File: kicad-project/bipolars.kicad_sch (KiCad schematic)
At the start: 16 parts, among them J13 Conn_01x04_Male, J14 Conn_01x04_Male, J4 Conn_01x02_Female, J5 Conn_01x02_Female, J6 Conn_01x02_Female, J7 Conn_01x04_Male, J8 Conn_01x04_Male, J9 Conn_01x02_Female, U5 A4988_Shield, U6 A4988_Shield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

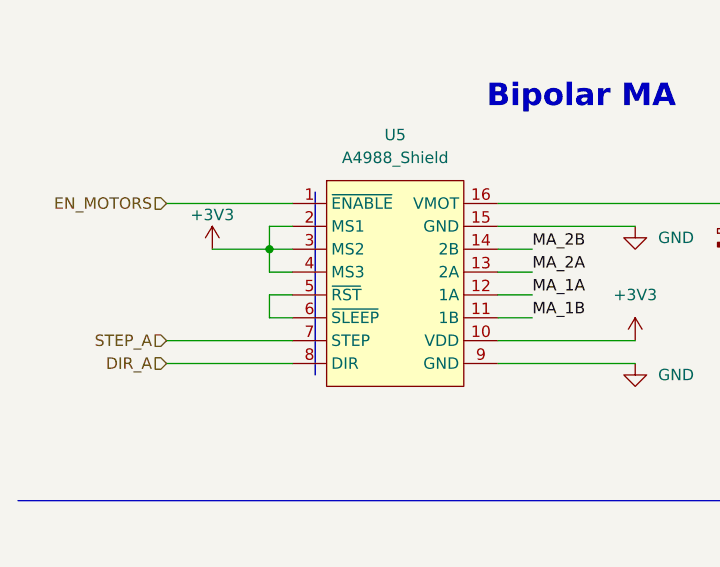
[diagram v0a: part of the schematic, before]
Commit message: hw: HSD v1.0 w/out peripherals
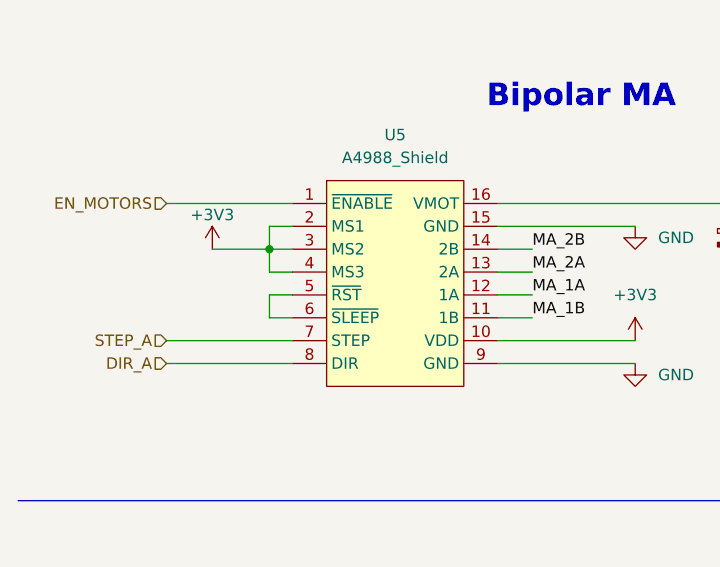
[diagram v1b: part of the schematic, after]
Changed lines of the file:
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@@
     (stroke (width 0) (type default) (color 0 0 0 0))
-  )
-  (polyline (pts (xy 46.99 63.5) (xy 46.99 43.18))
-    (stroke (width 0) (type solid) (color 255 45 140 1))
   )
   (wire (pts (xy 30.48 115.57) (xy 44.45 115.57))
